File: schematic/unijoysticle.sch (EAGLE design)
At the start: 6 parts, among them IC1 4066N, IC2 4066N, IC3 4066N, J1 DB9, J2 DB9

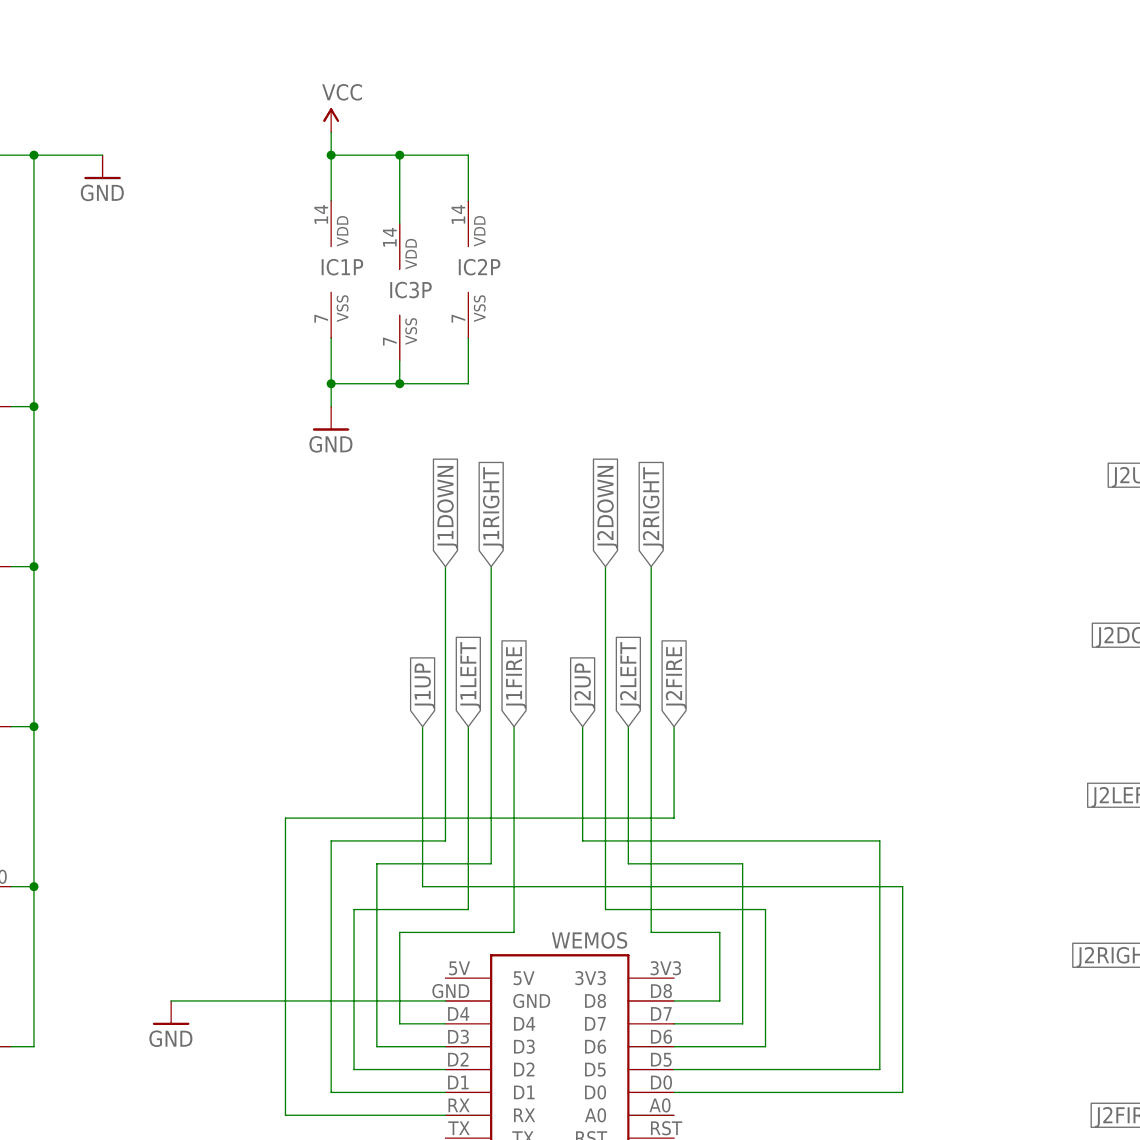
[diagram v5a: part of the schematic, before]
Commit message: board: add 5V barrel jack to board (again)
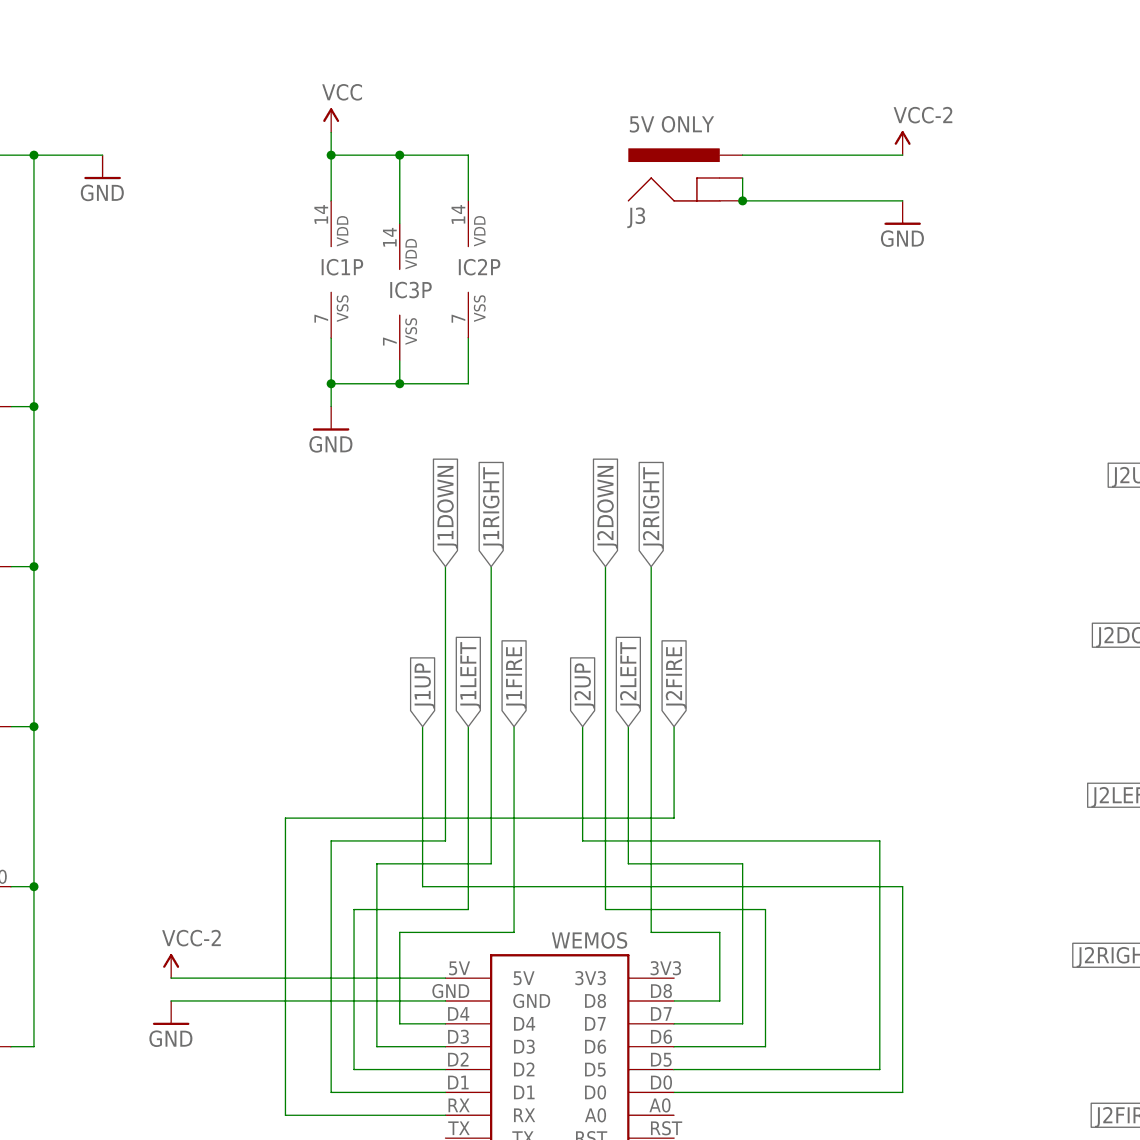
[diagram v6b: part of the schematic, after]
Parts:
- added J3: 5V ONLY, SparkFun-Connectors:POWER_JACKSLT
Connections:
- new net 5V: J3.PWR, U$1.5V
- net GND: now also J3.GND, J3.GNDBREAK
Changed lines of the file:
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@@
 <attributes>
 <attribute name="CNAME" value="Retro Moe"/>
-<attribute name="CREVISION" value="0.3.2"/>
+<attribute name="CREVISION" value="0.4.0"/>
 <attribute name="DESIGNER" value="Ricardo Quesada"/>
 </attributes>
@@
 <clearance class="0" value="0.254"/>
 </class>
-<class number="1" name="PWR5" width="0" drill="0">
+<class number="1" name="PWR5" width="0.3048" drill="0.508">
+<clearance class="1" value="0.254"/>
 </class>
 </classes>
@@
 <part name="GND6" library="SparkFun-Aesthetics" deviceset="GND" device=""/>
 <part name="U$1" library="1455413453956-wemos" deviceset="WEMOS" device=""/>
+<part name="J3" library="SparkFun-Connectors" deviceset="POWER_JACK" device="SLT" value="5V ONLY  "/>
+<part name="GND1" library="supply1" deviceset="GND" device=""/>
+<part name="SUPPLY1" library="SparkFun-Aesthetics" deviceset="VCC" device="" value="VCC-2"/>
+<part name="SUPPLY2" library="SparkFun-Aesthetics" deviceset="VCC" device="" value="VCC-2"/>
 </parts>
 <sheets>
@@
 <instance part="GND6" gate="1" x="76.2" y="152.4"/>
 <instance part="U$1" gate="G$1" x="134.62" y="66.04" rot="R180"/>
+<instance part="J3" gate="G$1" x="144.78" y="147.32"/>
+<instance part="GND1" gate="1" x="165.1" y="147.32"/>
+<instance part="SUPPLY1" gate="G$1" x="83.82" y="63.5"/>
+<instance part="SUPPLY2" gate="G$1" x="165.1" y="154.94"/>
 </instances>
 <busses>
@@
 <pinref part="GND6" gate="1" pin="GND"/>
 </segment>
+<segment>
+<pinref part="J3" gate="G$1" pin="GND"/>
+<wire x1="147.32" y1="149.86" x2="165.1" y2="149.86" width="0.1524" layer="91"/>
+<pinref part="GND1" gate="1" pin="GND"/>
+<pinref part="J3" gate="G$1" pin="GNDBREAK"/>
+<wire x1="147.32" y1="152.4" x2="147.32" y2="149.86" width="0.1524" layer="91"/>
+<junction x="147.32" y="149.86"/>
+</segment>
 </net>
 <net name="VCC" class="0">
@@
 </segment>
 </net>
+<net name="5V" class="0">
+<segment>
+<pinref part="U$1" gate="G$1" pin="5V"/>
+<wire x1="83.82" y1="63.5" x2="114.3" y2="63.5" width="0.1524" layer="91"/>
+<pinref part="SUPPLY1" gate="G$1" pin="VCC"/>
+</segment>
+<segment>
+<pinref part="J3" gate="G$1" pin="PWR"/>
+<wire x1="147.32" y1="154.94" x2="165.1" y2="154.94" width="0.1524" layer="91"/>
+<pinref part="SUPPLY2" gate="G$1" pin="VCC"/>
+</segment>
+</net>

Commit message: board: missing via and better labels
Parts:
- J3: value 5V ONLY -> POWER
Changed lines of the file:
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@@
 <part name="GND6" library="SparkFun-Aesthetics" deviceset="GND" device=""/>
 <part name="U$1" library="1455413453956-wemos" deviceset="WEMOS" device=""/>
-<part name="J3" library="SparkFun-Connectors" deviceset="POWER_JACK" device="SLT" value="5V ONLY  "/>
+<part name="J3" library="SparkFun-Connectors" deviceset="POWER_JACK" device="SLT" value="POWER"/>
 <part name="GND1" library="supply1" deviceset="GND" device=""/>
 <part name="SUPPLY1" library="SparkFun-Aesthetics" deviceset="VCC" device="" value="VCC-2"/>

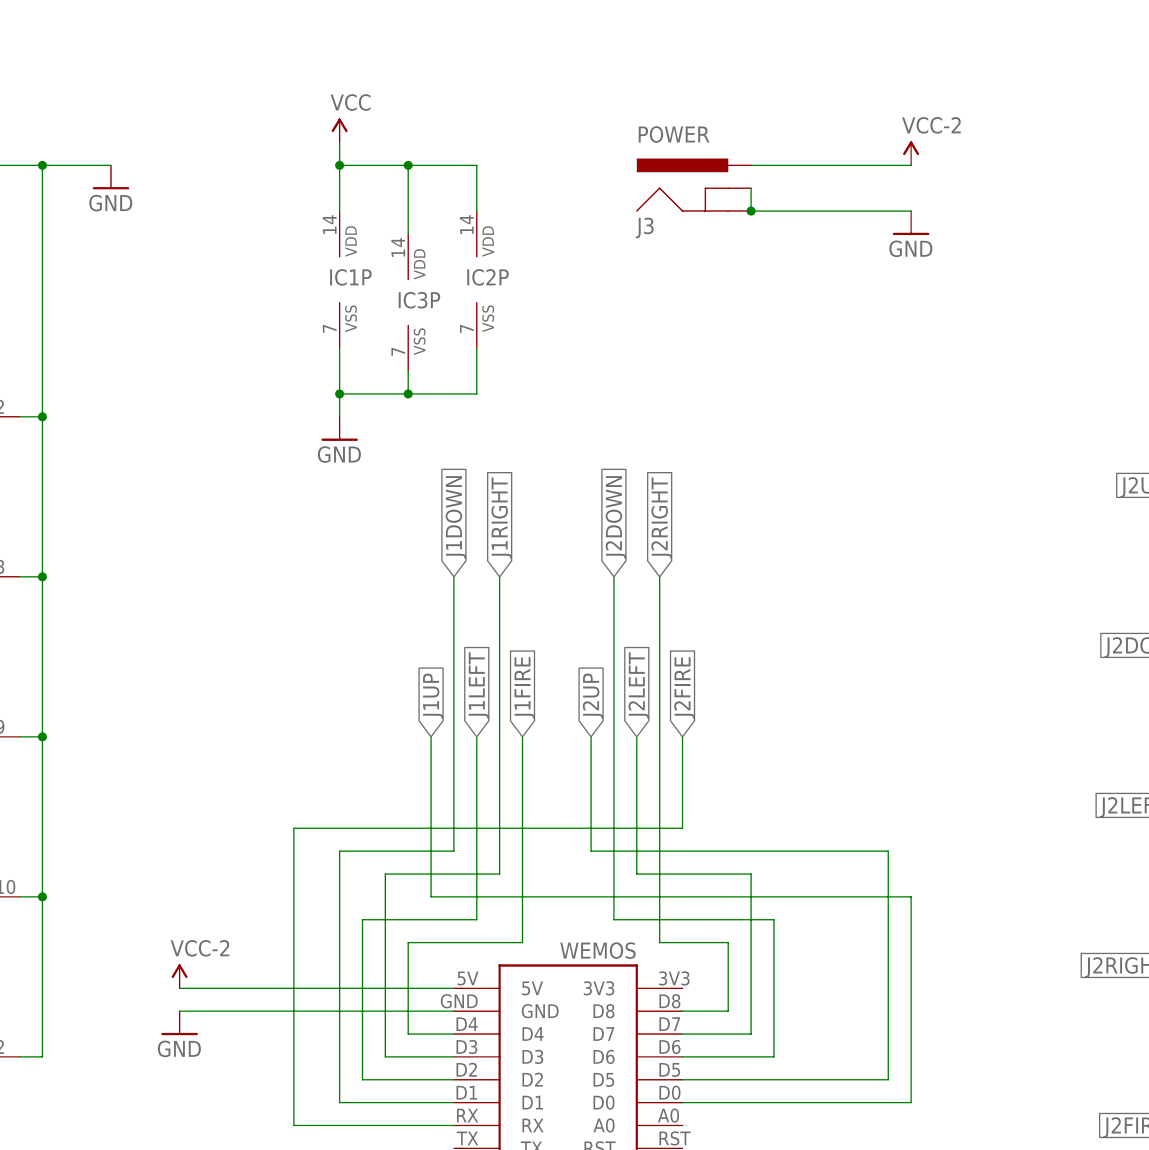
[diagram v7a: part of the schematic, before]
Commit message: schematic: adds diode again
I don't know if it is really needed, but it is scary
to see the c64 LED on, even if the computer is off
when the unijosyticle is being powered by USB,
but externally connected to the datassette port
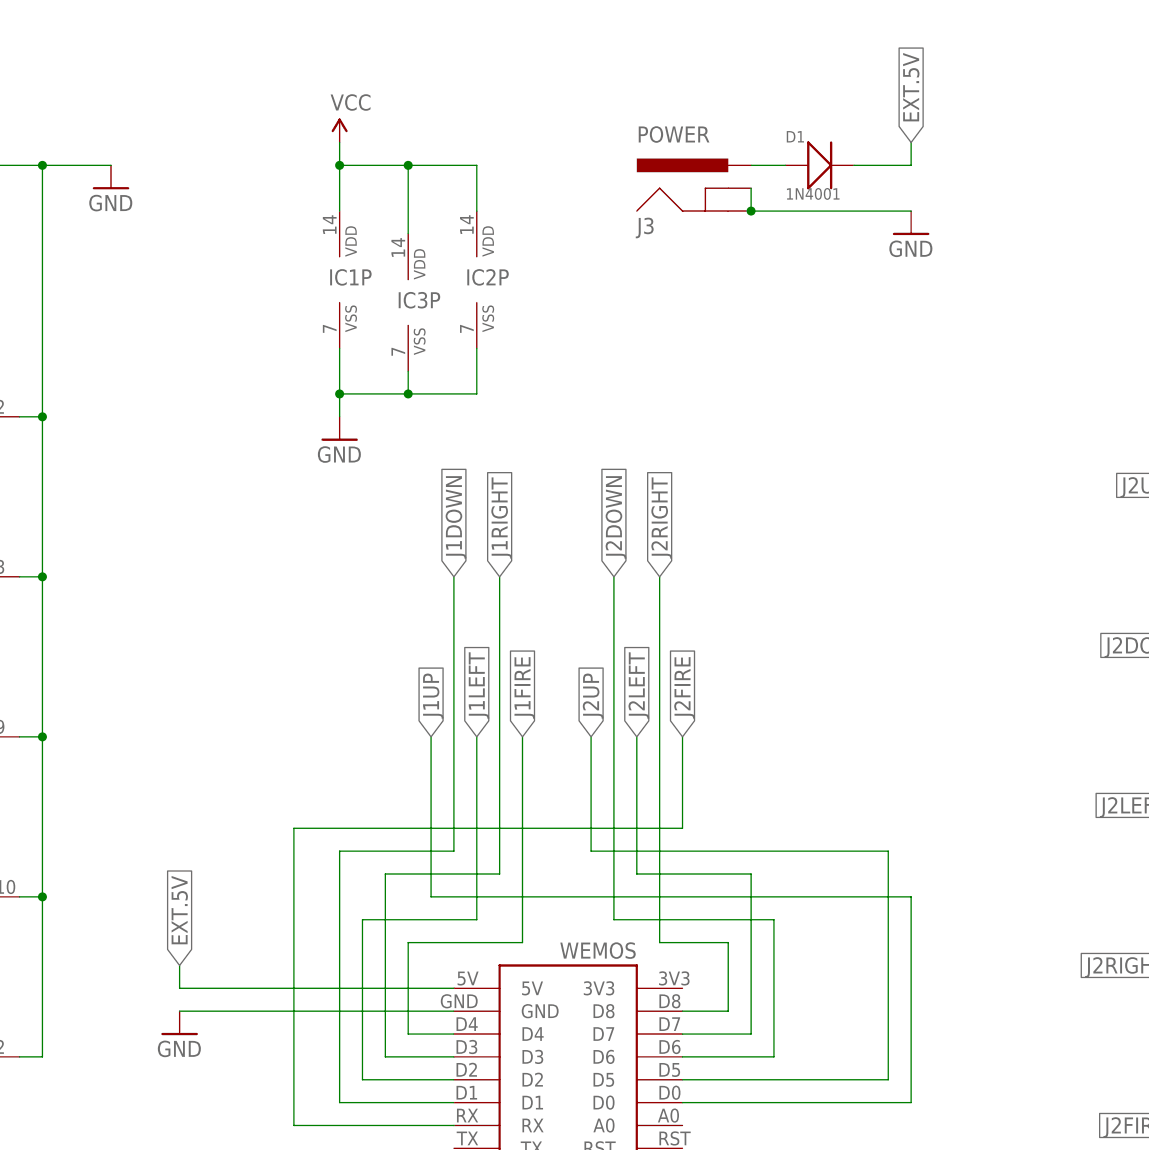
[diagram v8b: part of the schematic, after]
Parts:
- added D1: 1N4001, Seeed-OPL-Diode:DIP-DIODE-50V-1A-1N4001(DO-41)
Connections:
- removed net 5V: J3.PWR, U$1.5V
- new net EXT.5V: D1.-, U$1.5V
- new net N$1: D1.+, J3.PWR
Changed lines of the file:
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@@
 <?xml version="1.0" encoding="utf-8"?>
 <!DOCTYPE eagle SYSTEM "eagle.dtd">
-<eagle version="7.6.0">
+<eagle version="7.7.0">
 <drawing>
 <settings>
@@
 <layer number="115" name="ReferenceISLANDS" color="7" fill="1" visible="yes" active="yes"/>
 <layer number="116" name="Patch_BOT" color="9" fill="4" visible="yes" active="yes"/>
+<layer number="117" name="BACKMAAT1" color="7" fill="1" visible="yes" active="yes"/>
 <layer number="118" name="Rect_Pads" color="7" fill="1" visible="yes" active="yes"/>
+<layer number="119" name="KAP_TEKEN" color="7" fill="1" visible="yes" active="yes"/>
+<layer number="120" name="KAP_MAAT1" color="7" fill="1" visible="yes" active="yes"/>
 <layer number="121" name="_tsilk" color="7" fill="1" visible="yes" active="yes"/>
 <layer number="122" name="_bsilk" color="7" fill="1" visible="yes" active="yes"/>
@@
 <layer number="128" name="_bValues" color="7" fill="1" visible="yes" active="yes"/>
 <layer number="129" name="Mask" color="7" fill="1" visible="yes" active="yes"/>
+<layer number="130" name="SMDSTROOK" color="7" fill="1" visible="yes" active="yes"/>
 <layer number="131" name="tAdjust" color="7" fill="1" visible="yes" active="yes"/>
 <layer number="132" name="bAdjust" color="7" fill="1" visible="yes" active="yes"/>
@@
 <attributes>
 <attribute name="CNAME" value="Retro Moe"/>
-<attribute name="CREVISION" value="0.4.0"/>
+<attribute name="CREVISION" value="0.4.1"/>
 <attribute name="DESIGNER" value="Ricardo Quesada"/>
 </attributes>
@@
 <part name="J3" library="SparkFun-Connectors" deviceset="POWER_JACK" device="SLT" value="POWER"/>
 <part name="GND1" library="supply1" deviceset="GND" device=""/>
-<part name="SUPPLY1" library="SparkFun-Aesthetics" deviceset="VCC" device="" value="VCC-2"/>
-<part name="SUPPLY2" library="SparkFun-Aesthetics" deviceset="VCC" device="" value="VCC-2"/>
+<part name="D1" library="Seeed-OPL-Diode" deviceset="DIP-DIODE-50V-1A-1N4001(DO-41)" device="" value="1N4001"/>
 </parts>
 <sheets>
@@
 <instance part="J3" gate="G$1" x="144.78" y="147.32"/>
 <instance part="GND1" gate="1" x="165.1" y="147.32"/>
-<instance part="SUPPLY1" gate="G$1" x="83.82" y="63.5"/>
-<instance part="SUPPLY2" gate="G$1" x="165.1" y="154.94"/>
+<instance part="D1" gate="G$1" x="154.94" y="154.94"/>
 </instances>
 <busses>
@@
 </segment>
 </net>
-<net name="5V" class="0">
+<net name="N$1" class="0">
+<segment>
+<pinref part="J3" gate="G$1" pin="PWR"/>
+<wire x1="147.32" y1="154.94" x2="151.13" y2="154.94" width="0.1524" layer="91"/>
+<pinref part="D1" gate="G$1" pin="+"/>
+</segment>
+</net>
+<net name="EXT.5V" class="0">
 <segment>
 <pinref part="U$1" gate="G$1" pin="5V"/>
-<wire x1="83.82" y1="63.5" x2="114.3" y2="63.5" width="0.1524" layer="91"/>
-<pinref part="SUPPLY1" gate="G$1" pin="VCC"/>
-</segment>
-<segment>
-<pinref part="J3" gate="G$1" pin="PWR"/>
-<wire x1="147.32" y1="154.94" x2="165.1" y2="154.94" width="0.1524" layer="91"/>
-<pinref part="SUPPLY2" gate="G$1" pin="VCC"/>
-</segment>
-</net>
+<wire x1="114.3" y1="63.5" x2="83.82" y2="63.5" width="0.1524" layer="91"/>
+<wire x1="83.82" y1="63.5" x2="83.82" y2="66.04" width="0.1524" layer="91"/>
+<label x="83.82" y="66.04" size="1.778" layer="95" rot="R90" xref="yes"/>
+</segment>
+<segment>
+<wire x1="158.75" y1="154.94" x2="165.1" y2="154.94" width="0.1524" layer="91"/>
+<wire x1="165.1" y1="154.94" x2="165.1" y2="157.48" width="0.1524" layer="91"/>
+<label x="165.1" y="157.48" size="1.778" layer="95" rot="R90" xref="yes"/>
+<pinref part="D1" gate="G$1" pin="-"/>
+</segment>
+</net>
